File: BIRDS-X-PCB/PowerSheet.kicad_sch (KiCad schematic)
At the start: 22 parts, among them J201 Conn_01x02, J202 Conn_01x02, J203 Conn_01x02, Q201 AO3420, Q202 AO3420, U201 LTC4361-2, U202 LTC4361-2, U203 0.1S7B_0512S3UP

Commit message: Update footprints to 0603
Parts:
- C201, C202, C203, C204: footprint Capacitor_SMD:C_0805_2012Metric_Pad1.18x1.45mm_HandSolder -> Capacitor_SMD:C_0603_1608Metric_Pad1.08x0.95mm_HandSolder
- J201, J202, J203: footprint Connector_PinHeader_2.54mm:PinHeader_1x02_P2.54mm_Vertical -> Connector_PinHeader_1.27mm:PinHeader_1x02_P1.27mm_Vertical
- R203, R204, R205: footprint Resistor_SMD:R_0805_2012Metric_Pad1.20x1.40mm_HandSolder -> Resistor_SMD:R_0603_1608Metric_Pad0.98x0.95mm_HandSolder
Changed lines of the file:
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@@
       (effects (font (size 1.27 1.27)) (justify left))
     )
-    (property "Footprint" "Capacitor_SMD:C_0805_2012Metric_Pad1.18x1.45mm_HandSolder" (at 122.8852 53.34 0)
+    (property "Footprint" "Capacitor_SMD:C_0603_1608Metric_Pad1.08x0.95mm_HandSolder" (at 122.8852 53.34 0)
       (effects (font (size 1.27 1.27)) hide)
     )
@@
       (effects (font (size 1.27 1.27)) (justify left))
     )
-    (property "Footprint" "Capacitor_SMD:C_0805_2012Metric_Pad1.18x1.45mm_HandSolder" (at 181.3052 74.93 0)
+    (property "Footprint" "Capacitor_SMD:C_0603_1608Metric_Pad1.08x0.95mm_HandSolder" (at 181.3052 74.93 0)
       (effects (font (size 1.27 1.27)) hide)
     )
@@
       (effects (font (size 1.27 1.27)) (justify left))
     )
-    (property "Footprint" "Resistor_SMD:R_0805_2012Metric_Pad1.20x1.40mm_HandSolder" (at 211.582 130.81 90)
+    (property "Footprint" "Resistor_SMD:R_0603_1608Metric_Pad0.98x0.95mm_HandSolder" (at 211.582 130.81 90)
       (effects (font (size 1.27 1.27)) hide)
     )
@@
       (effects (font (size 1.27 1.27)) (justify left))
     )
-    (property "Footprint" "Capacitor_SMD:C_0805_2012Metric_Pad1.18x1.45mm_HandSolder" (at 124.1552 125.73 0)
+    (property "Footprint" "Capacitor_SMD:C_0603_1608Metric_Pad1.08x0.95mm_HandSolder" (at 124.1552 125.73 0)
       (effects (font (size 1.27 1.27)) hide)
     )
@@
       (effects (font (size 1.27 1.27)) (justify left))
     )
-    (property "Footprint" "Resistor_SMD:R_0805_2012Metric_Pad1.20x1.40mm_HandSolder" (at 196.342 130.81 90)
+    (property "Footprint" "Resistor_SMD:R_0603_1608Metric_Pad0.98x0.95mm_HandSolder" (at 196.342 130.81 90)
       (effects (font (size 1.27 1.27)) hide)
     )
@@
       (effects (font (size 1.27 1.27)) (justify left) hide)
     )
-    (property "Footprint" "Connector_PinHeader_2.54mm:PinHeader_1x02_P2.54mm_Vertical" (at 180.34 144.78 0)
+    (property "Footprint" "Connector_PinHeader_1.27mm:PinHeader_1x02_P1.27mm_Vertical" (at 180.34 144.78 0)
       (effects (font (size 1.27 1.27)) hide)
     )
@@
       (effects (font (size 1.27 1.27)) (justify left))
     )
-    (property "Footprint" "Capacitor_SMD:C_0805_2012Metric_Pad1.18x1.45mm_HandSolder" (at 228.2952 76.2 0)
+    (property "Footprint" "Capacitor_SMD:C_0603_1608Metric_Pad1.08x0.95mm_HandSolder" (at 228.2952 76.2 0)
       (effects (font (size 1.27 1.27)) hide)
     )
@@
       (effects (font (size 1.27 1.27)) (justify left) hide)
     )
-    (property "Footprint" "Connector_PinHeader_2.54mm:PinHeader_1x02_P2.54mm_Vertical" (at 180.34 106.68 0)
+    (property "Footprint" "Connector_PinHeader_1.27mm:PinHeader_1x02_P1.27mm_Vertical" (at 180.34 106.68 0)
       (effects (font (size 1.27 1.27)) hide)
     )
@@
       (effects (font (size 1.27 1.27)) (justify left))
     )
-    (property "Footprint" "Resistor_SMD:R_0805_2012Metric_Pad1.20x1.40mm_HandSolder" (at 226.822 130.81 90)
+    (property "Footprint" "Resistor_SMD:R_0603_1608Metric_Pad0.98x0.95mm_HandSolder" (at 226.822 130.81 90)
       (effects (font (size 1.27 1.27)) hide)
     )
@@
       (effects (font (size 1.27 1.27)) (justify left) hide)
     )
-    (property "Footprint" "Connector_PinHeader_2.54mm:PinHeader_1x02_P2.54mm_Vertical" (at 180.34 125.73 0)
-      (effects (font (size 1.27 1.27)) hide)
-    )
+    (property "Footprint" "Connector_PinHeader_1.27mm:PinHeader_1x02_P1.27mm_Vertical" (at 180.34 125.73 0)
+      (effects (font (size 1.27 1.27)) hide)
+    )

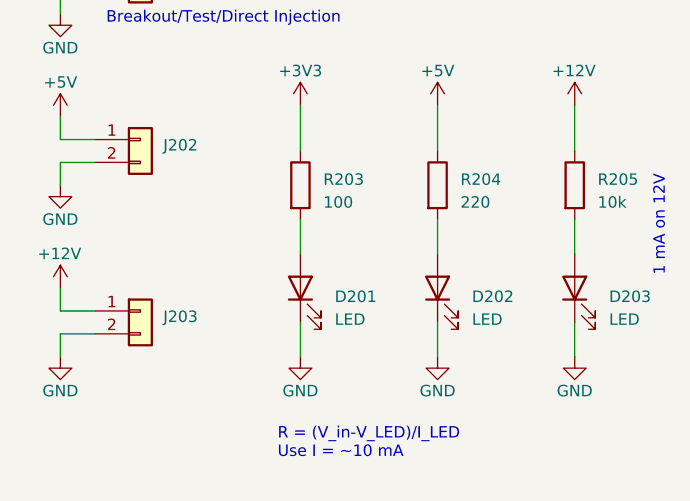
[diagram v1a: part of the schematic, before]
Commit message: Add MCU assignments, RF annotations per ref design, heirarchal pins
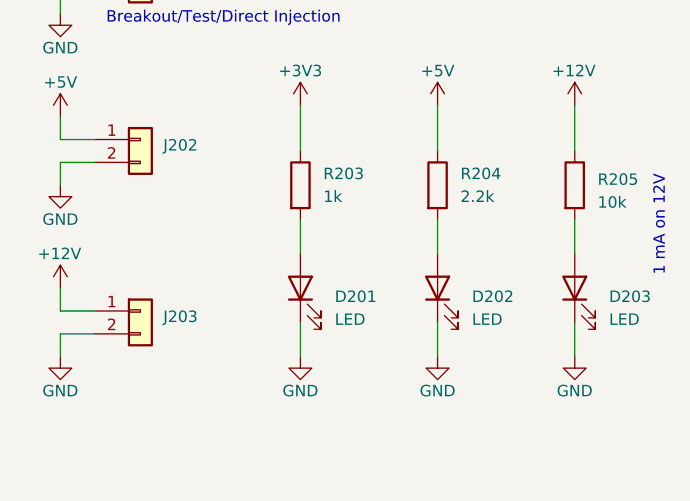
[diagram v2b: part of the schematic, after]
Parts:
- R203: value 100 -> 1k
- R204: value 220 -> 2.2k
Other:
- note removed: "R = (V_in-V_LED)/I_LED Use I = ~10 mA"
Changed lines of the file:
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@@
     (stroke (width 0) (type default))
-  )
-  (text "R = (V_in-V_LED)/I_LED\nUse I = ~10 mA" (at 195.58 161.29 0)
-    (effects (font (size 1.27 1.27)) (justify left bottom))
   )
   (text "Breakout/Test/Direct Injection" (at 176.53 113.03 0)
@@
   (symbol (lib_id "Device:R") (at 213.36 130.81 0) (unit 1)
     (in_bom yes) (on_board yes) (dnp no) (fields_autoplaced)
-    (property "Reference" "R204" (at 215.9 130.175 0)
-      (effects (font (size 1.27 1.27)) (justify left))
-    )
-    (property "Value" "220" (at 215.9 132.715 0)
+    (property "Reference" "R204" (at 215.9 129.54 0)
+      (effects (font (size 1.27 1.27)) (justify left))
+    )
+    (property "Value" "2.2k" (at 215.9 132.08 0)
       (effects (font (size 1.27 1.27)) (justify left))
     )
@@
   (symbol (lib_id "Device:R") (at 198.12 130.81 0) (unit 1)
     (in_bom yes) (on_board yes) (dnp no) (fields_autoplaced)
-    (property "Reference" "R203" (at 200.66 130.175 0)
-      (effects (font (size 1.27 1.27)) (justify left))
-    )
-    (property "Value" "100" (at 200.66 132.715 0)
-      (effects (font (size 1.27 1.27)) (justify left))
-    )
+    (property "Reference" "R203" (at 200.66 129.54 0)
+      (effects (font (size 1.27 1.27)) (justify left))
+    )
+    (property "Value" "1k" (at 200.66 132.08 0)
+      (effects (font (size 1.27 1.27)) (justify left))
+    )

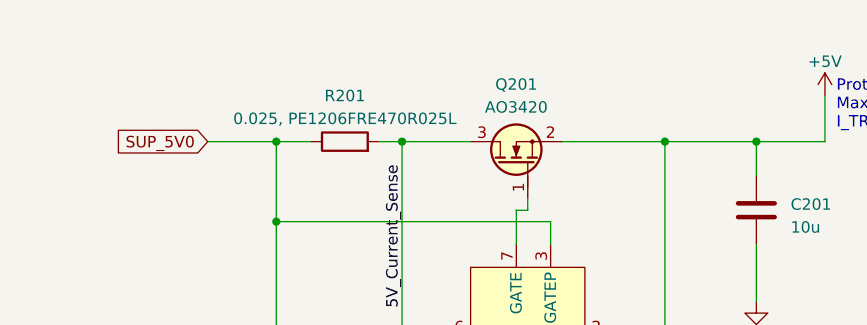
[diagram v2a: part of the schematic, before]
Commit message: Finish most routing
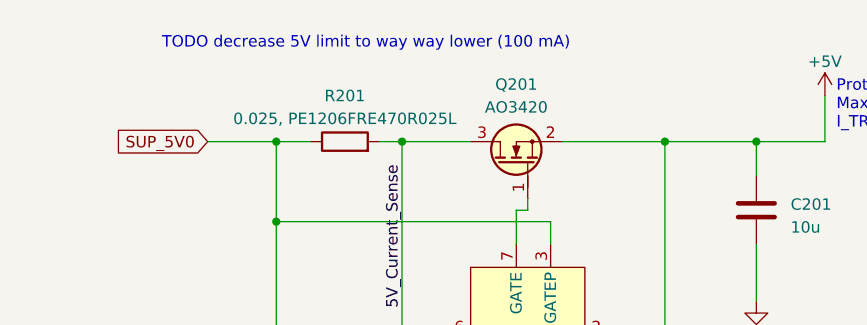
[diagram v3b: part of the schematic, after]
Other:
- note added: "TODO decrease 5V limit to way way lower (100 mA)"
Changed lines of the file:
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@@
+    (effects (font (size 1.27 1.27)) (justify left bottom))
+  )
+  (text "TODO decrease 5V limit to way way lower (100 mA)" (at 55.88 31.75 0)
     (effects (font (size 1.27 1.27)) (justify left bottom))
   )

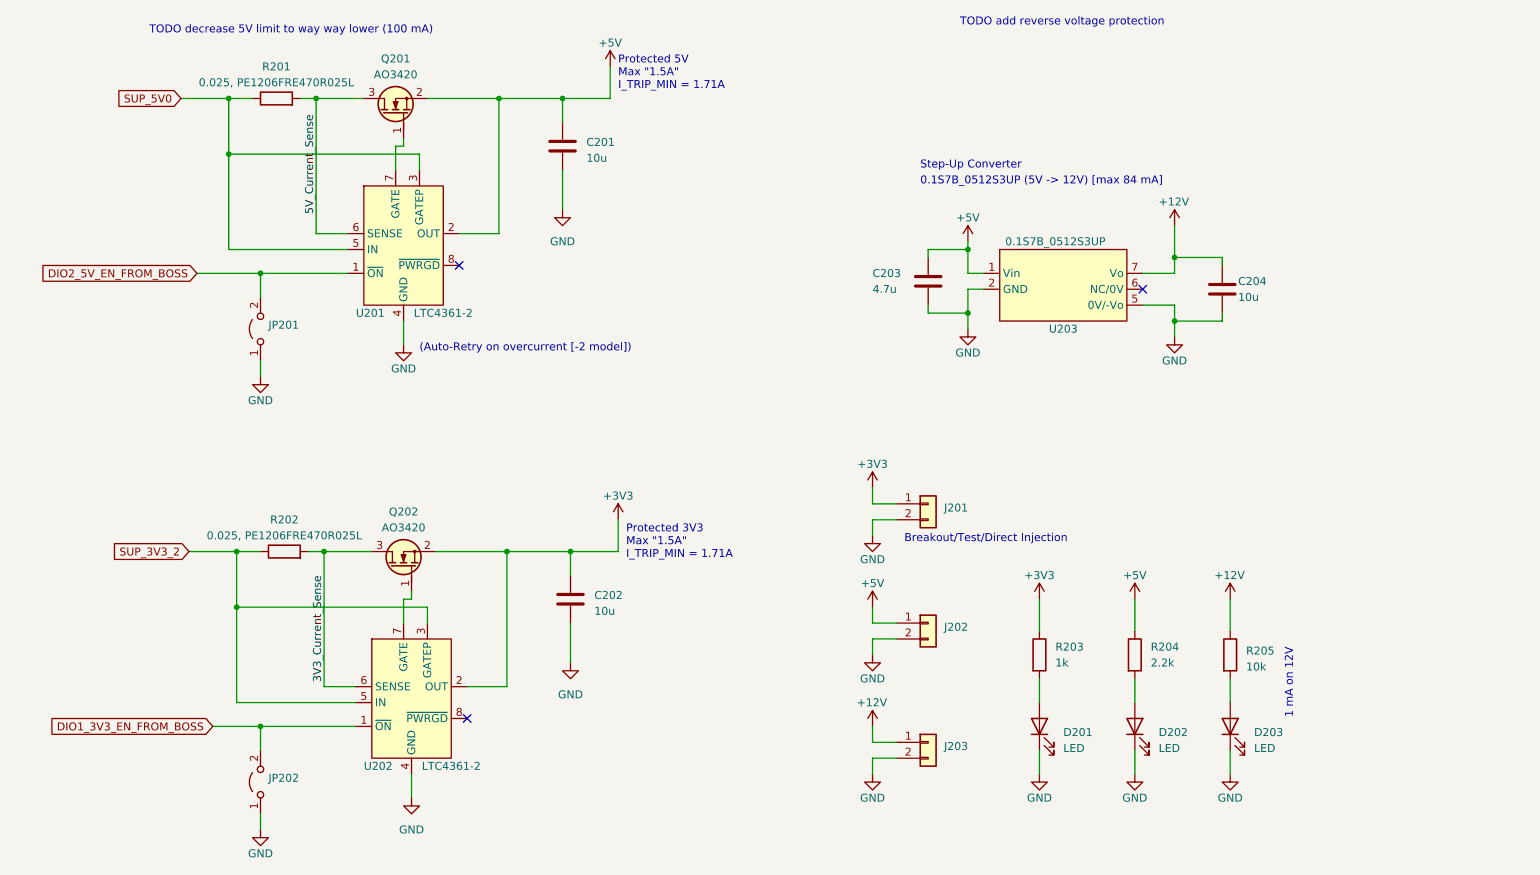
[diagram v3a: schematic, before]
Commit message: Add EMC protection for 12V step-up
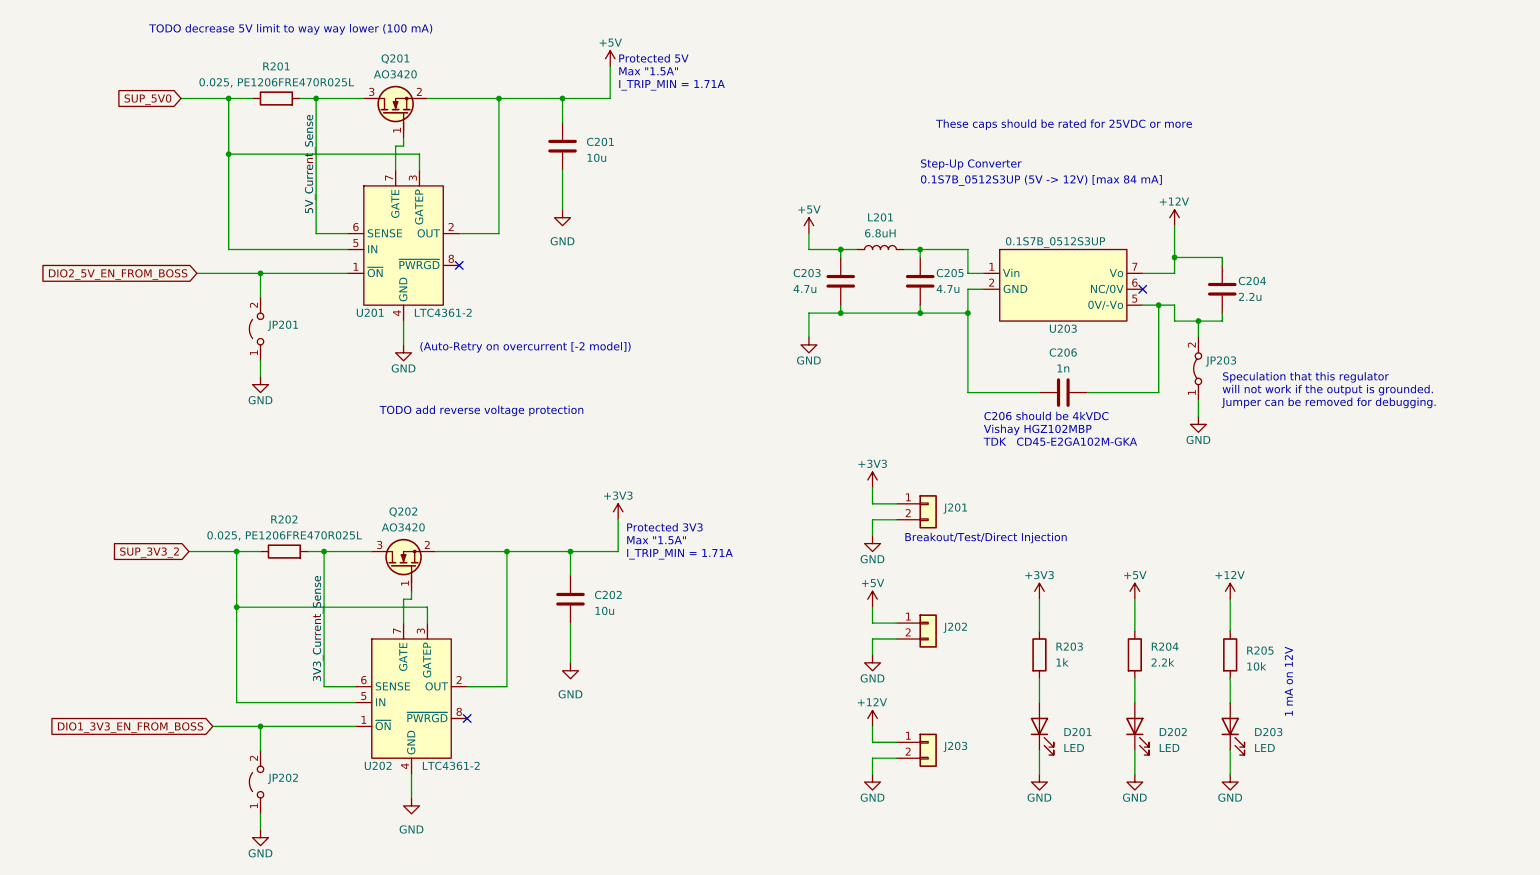
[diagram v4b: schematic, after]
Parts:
- added C205: 4.7u, Capacitor_SMD:C_0603_1608Metric_Pad1.08x0.95mm_HandSolder, symbol Device:C
- added C206: 1n, Capacitor_SMD:C_0603_1608Metric_Pad1.08x0.95mm_HandSolder, symbol Device:C
- added JP203: Jumper_2_Bridged, Jumper:SolderJumper-2_P1.3mm_Open_RoundedPad1.0x1.5mm, symbol Jumper:Jumper_2_Bridged
- added L201: 6.8uH, Inductor_SMD:L_0603_1608Metric_Pad1.05x0.95mm_HandSolder, symbol Device:L
- C204: value 10u -> 2.2u
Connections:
- net +5V: now also L201.1; no longer U203.1 (Vin)
- net GND: now also C205.2, C206.2, JP203.1 (A); no longer C204.2, U203.5 (0V/-Vo)
- new net: C204.2, C206.1, JP203.2 (B), U203.5 (0V/-Vo)
- new net: C205.1, L201.2, U203.1 (Vin)
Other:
- note added: "C206 should be 4kVDC Vishay HGZ102MBP TDK CD45-E2GA102M-GKA"
- note added: "Speculation that this regulator will not work if the output is grounded. Jumper can be removed for debugging."
- note added: "These caps should be rated for 25VDC or more"
- moved on the sheet: C203

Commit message: Clean up NucleoTNC
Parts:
- added C207, C208: 1u, Capacitor_SMD:C_0603_1608Metric_Pad1.08x0.95mm_HandSolder, symbol Device:C
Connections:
- net +3V3: now also C207.1
- net +5V: now also C208.1
- net GND: now also C207.2, C208.2
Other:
- moved on the sheet: C202

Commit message: Clean up heirarchy
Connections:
- net SUP_3V3_2 renamed SUP_3V3
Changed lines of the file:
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@@
     (effects (font (size 1.27 1.27)) (justify right bottom))
   )
-  (global_label "DIO1_3V3_EN_FROM_BOSS" (shape input) (at 66.04 142.24 180) (fields_autoplaced)
+  (hierarchical_label "DIO2_5V_EN_FROM_BOSS" (shape input) (at 63.5 69.85 180) (fields_autoplaced)
     (effects (font (size 1.27 1.27)) (justify right))
-    (property "Intersheetrefs" "${INTERSHEET_REFS}" (at 38.7019 142.24 0)
-      (effects (font (size 1.27 1.27)) (justify right) hide)
-    )
   )
-  (global_label "SUP_3V3_2" (shape input) (at 62.23 114.3 180) (fields_autoplaced)
+  (hierarchical_label "DIO1_3V3_EN_FROM_BOSS" (shape input) (at 66.04 142.24 180) (fields_autoplaced)
     (effects (font (size 1.27 1.27)) (justify right))
-    (property "Intersheetrefs" "${INTERSHEET_REFS}" (at 48.8619 114.3 0)
-      (effects (font (size 1.27 1.27)) (justify right) hide)
-    )
   )
-  (global_label "SUP_5V0" (shape input) (at 60.96 41.91 180) (fields_autoplaced)
+  (hierarchical_label "SUP_3V3" (shape input) (at 62.23 114.3 180) (fields_autoplaced)
     (effects (font (size 1.27 1.27)) (justify right))
-    (property "Intersheetrefs" "${INTERSHEET_REFS}" (at 49.769 41.91 0)
-      (effects (font (size 1.27 1.27)) (justify right) hide)
-    )
   )
-  (global_label "DIO2_5V_EN_FROM_BOSS" (shape input) (at 63.5 69.85 180) (fields_autoplaced)
+  (hierarchical_label "SUP_5V0" (shape input) (at 60.96 41.91 180) (fields_autoplaced)
     (effects (font (size 1.27 1.27)) (justify right))
-    (property "Intersheetrefs" "${INTERSHEET_REFS}" (at 37.3714 69.85 0)
-      (effects (font (size 1.27 1.27)) (justify right) hide)
-    )
   )
   (symbol (lib_id "power:GND") (at 128.27 59.69 0) (unit 1)

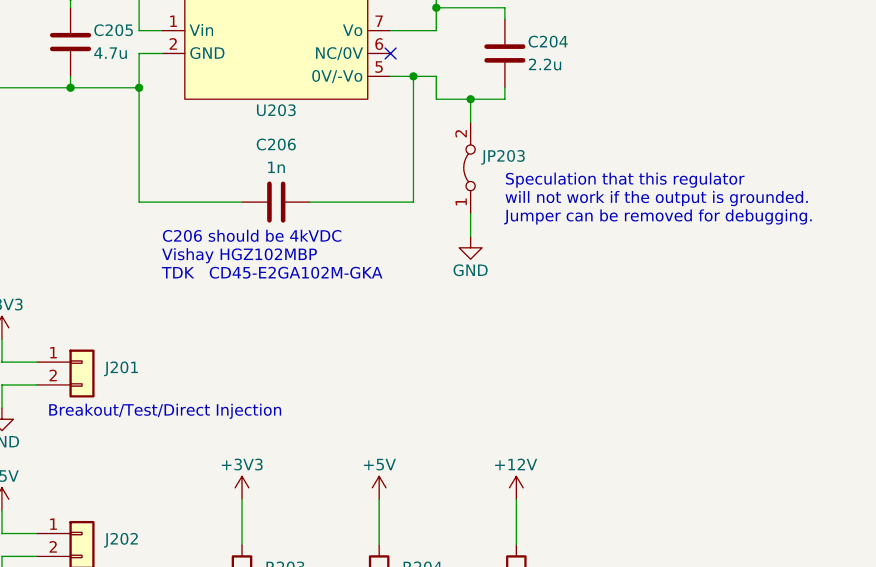
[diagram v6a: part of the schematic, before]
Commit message: Schematic updates
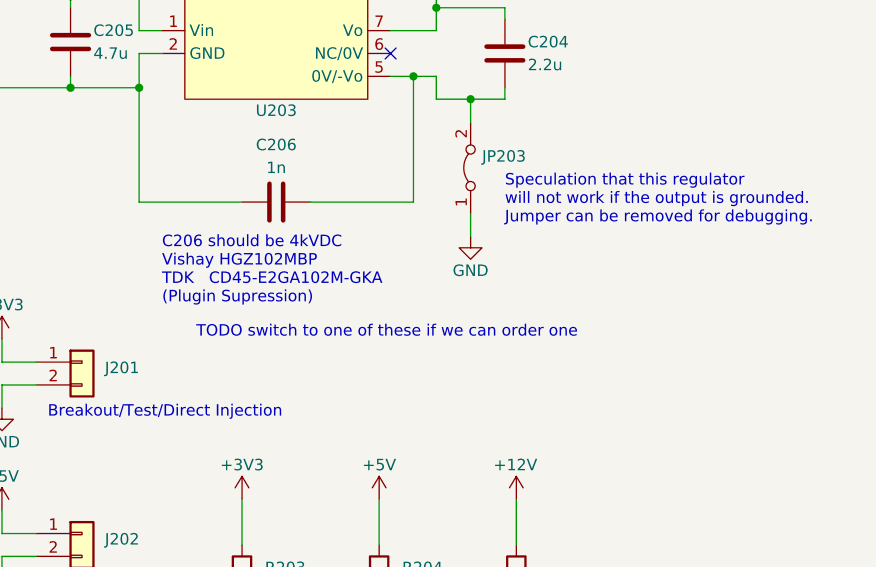
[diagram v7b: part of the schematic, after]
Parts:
- C206: footprint Capacitor_SMD:C_0603_1608Metric_Pad1.08x0.95mm_HandSolder -> Capacitor_SMD:C_1812_4532Metric; LCSC (none) -> C524544
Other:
- note added: "C206 should be 4kVDC Vishay HGZ102MBP TDK CD45-E2GA102M-GKA (Plugin Supression)"
- note added: "TODO switch to one of these if we can order one"
- note removed: "C206 should be 4kVDC Vishay HGZ102MBP TDK CD45-E2GA102M-GKA"
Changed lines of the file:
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@@
     (stroke (width 0) (type default))
   )
-  (text "C206 should be 4kVDC\nVishay HGZ102MBP\nTDK   CD45-E2GA102M-GKA"
-    (at 189.23 97.79 0)
+  (text "C206 should be 4kVDC\nVishay HGZ102MBP\nTDK   CD45-E2GA102M-GKA\n(Plugin Supression)"
+    (at 189.23 100.33 0)
+    (effects (font (size 1.27 1.27)) (justify left bottom))
+  )
+  (text "TODO switch to one of these if we can order one" (at 193.04 104.14 0)
     (effects (font (size 1.27 1.27)) (justify left bottom))
   )
@@
       (effects (font (size 1.27 1.27)))
     )
-    (property "Footprint" "Capacitor_SMD:C_0603_1608Metric_Pad1.08x0.95mm_HandSolder" (at 198.12 89.8652 0)
-      (effects (font (size 1.27 1.27)) hide)
-    )
-    (property "Datasheet" "~" (at 201.93 88.9 0)
-      (effects (font (size 1.27 1.27)) hide)
-    )
+    (property "Footprint" "Capacitor_SMD:C_1812_4532Metric" (at 198.12 89.8652 0)
+      (effects (font (size 1.27 1.27)) hide)
+    )
+    (property "Datasheet" "https://datasheet.lcsc.com/lcsc/2103290903_Murata-Electronics-GA342QR7GD102KW01L_C524544.pdf" (at 201.93 88.9 0)
+      (effects (font (size 1.27 1.27)) hide)
+    )
+    (property "LCSC" "C524544" (at 201.93 88.9 90)
+      (effects (font (size 1.27 1.27)) hide)
+    )

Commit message: Do most of routing
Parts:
- D201, D202, D203: footprint LED_SMD:LED_1206_3216Metric_Pad1.42x1.75mm_HandSolder -> LED_SMD:LED_0603_1608Metric
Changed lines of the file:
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@@
       (effects (font (size 1.27 1.27)) (justify right))
     )
-    (property "Footprint" "LED_SMD:LED_1206_3216Metric_Pad1.42x1.75mm_HandSolder" (at 213.36 142.24 0)
+    (property "Footprint" "LED_SMD:LED_0603_1608Metric" (at 213.36 142.24 0)
       (effects (font (size 1.27 1.27)) hide)
     )
@@
       (effects (font (size 1.27 1.27)) (justify right))
     )
-    (property "Footprint" "LED_SMD:LED_1206_3216Metric_Pad1.42x1.75mm_HandSolder" (at 198.12 142.24 0)
+    (property "Footprint" "LED_SMD:LED_0603_1608Metric" (at 198.12 142.24 0)
       (effects (font (size 1.27 1.27)) hide)
     )
@@
       (effects (font (size 1.27 1.27)) (justify right))
     )
-    (property "Footprint" "LED_SMD:LED_1206_3216Metric_Pad1.42x1.75mm_HandSolder" (at 228.6 142.24 0)
+    (property "Footprint" "LED_SMD:LED_0603_1608Metric" (at 228.6 142.24 0)
       (effects (font (size 1.27 1.27)) hide)
     )
